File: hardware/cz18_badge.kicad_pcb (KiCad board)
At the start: 2 copper layers, 100 x 100 mm, 16 parts, among them U1 NRF24L01_Breakout

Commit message: Added 433MHz modules
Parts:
- added RF1: RF_Receiver_433_MHz, Sensors:RF_Receiver_433_MHz, F.Cu at (143.5, 44.5)
- added RF2: RF_Transmitter_433_MHz, Sensors:RF_Transmitter_433_MHz, F.Cu at (53.3, 38.1)
- moved U1 54.5 mm to (67.3, 96.5)
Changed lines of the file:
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@@
     (tracks 0)
     (zones 0)
-    (modules 16)
-    (nets 43)
+    (modules 18)
+    (nets 50)
   )
   (page A4)
@@
   (net 41 "Net-(U1-Pad3)")
   (net 42 "Net-(U1-Pad4)")
+  (net 43 "Net-(RF1-Pad1)")
+  (net 44 "Net-(RF1-Pad2)")
+  (net 45 "Net-(RF1-Pad3)")
+  (net 46 "Net-(RF1-Pad4)")
+  (net 47 "Net-(RF2-Pad1)")
+  (net 48 "Net-(RF2-Pad2)")
+  (net 49 "Net-(RF2-Pad3)")
   (net_class Default "This is the default net class."
     (clearance 0.2)
@@
     (add_net "Net-(D3-Pad4)")
     (add_net "Net-(D4-Pad4)")
+    (add_net "Net-(RF1-Pad1)")
+    (add_net "Net-(RF1-Pad2)")
+    (add_net "Net-(RF1-Pad3)")
+    (add_net "Net-(RF1-Pad4)")
+    (add_net "Net-(RF2-Pad1)")
+    (add_net "Net-(RF2-Pad2)")
+    (add_net "Net-(RF2-Pad3)")
     (add_net "Net-(U1-Pad3)")
     (add_net "Net-(U1-Pad4)")
@@
   )
   (module mysensors_radios:NRF24L01 (layer F.Cu)
-    (at 100 140.075001)
+    (at 67.31 96.52)
     (descr NRF24L01)
     (tags "nRF 24 NRF24L01 NRF24L01+")
@@
     )
   )
+  (module Sensors:RF_Receiver_433_MHz (layer F.Cu)
+    (at 143.51 44.45 270)
+    (descr "433 MHz RF Receiver")
+    (tags "rf receiver 433 mhz")
+    (fp_text reference RF1 (at 0 -3 270) (layer F.SilkS)
+      (effects (font (size 1 1) (thickness 0.15)))
+    )
+    (fp_text value RF_Receiver_433_MHz (at 0 3 270) (layer F.Fab)
+      (effects (font (size 1 1) (thickness 0.15)))
+    )
+    (fp_line (start -4.7 -1.1) (end -4.7 -4.6) (layer F.CrtYd) (width 0.15))
+    (fp_line (start -7.4 -1.1) (end -4.7 -1.1) (layer F.CrtYd) (width 0.15))
+    (fp_line (start -7.4 -4.6) (end -7.4 -1.1) (layer F.CrtYd) (width 0.15))
+    (fp_circle (center -20.8 -3) (end -19.6 -2) (layer F.CrtYd) (width 0.15))
+    (fp_line (start 7.58 -4.55) (end 7.58 -5.55) (layer F.CrtYd) (width 0.15))
+    (fp_line (start -22.82 -4.55) (end 7.58 -4.55) (layer F.CrtYd) (width 0.15))
+    (fp_line (start -22.82 -5.54) (end -22.82 -4.55) (layer F.CrtYd) (width 0.15))
+    (fp_line (start 7.58 -5.54) (end -22.82 -5.54) (layer F.CrtYd) (width 0.15))
+    (fp_line (start -3.790707 1.294229) (end 3.829293 1.294229) (layer F.SilkS) (width 0.15))
+    (fp_line (start -3.790707 -1.245771) (end 3.829293 -1.245771) (layer F.SilkS) (width 0.15))
+    (fp_line (start -6.610707 -1.525771) (end -5.060707 -1.525771) (layer F.SilkS) (width 0.15))
+    (fp_line (start 3.829293 1.294229) (end 3.829293 -1.245771) (layer F.SilkS) (width 0.15))
+    (fp_line (start -3.790707 -1.245771) (end -3.790707 1.294229) (layer F.SilkS) (width 0.15))
+    (fp_line (start -5.060707 1.574229) (end -6.610707 1.574229) (layer F.SilkS) (width 0.15))
+    (fp_line (start -6.610707 1.574229) (end -6.610707 -1.525771) (layer F.SilkS) (width 0.15))
+    (pad 1 thru_hole rect (at -5.060707 0.024229) (size 2.032 1.7272) (drill 1.016) (layers *.Cu *.Mask F.SilkS)
+      (net 43 "Net-(RF1-Pad1)"))
+    (pad 2 thru_hole oval (at -2.520707 0.024229) (size 2.032 1.7272) (drill 1.016) (layers *.Cu *.Mask F.SilkS)
+      (net 44 "Net-(RF1-Pad2)"))
+    (pad 3 thru_hole oval (at 0.019293 0.024229) (size 2.032 1.7272) (drill 1.016) (layers *.Cu *.Mask F.SilkS)
+      (net 45 "Net-(RF1-Pad3)"))
+    (pad 4 thru_hole oval (at 2.559293 0.024229) (size 2.032 1.7272) (drill 1.016) (layers *.Cu *.Mask F.SilkS)
+      (net 46 "Net-(RF1-Pad4)"))
+    (model Pin_Headers.3dshapes/Pin_Header_Straight_1x04.wrl
+      (at (xyz 0 -0.15 0))
+      (scale (xyz 1 1 1))
+      (rotate (xyz 0 0 90))
+    )
+  )
+  (module Sensors:RF_Transmitter_433_MHz (layer F.Cu)
+    (at 53.34 38.1 90)
+    (fp_text reference RF2 (at 0 4.445 90) (layer F.SilkS)
+      (effects (font (size 1 1) (thickness 0.15)))
+    )
+    (fp_text value RF_Transmitter_433_MHz (at 0 2.54 90) (layer F.Fab)
+      (effects (font (size 1 1) (thickness 0.15)))
+    )
+    (fp_line (start 3.81 1.27) (end -1.27 1.27) (layer F.SilkS) (width 0.15))
+    (fp_line (start 3.81 -1.27) (end 3.81 1.27) (layer F.SilkS) (width 0.15))
+    (fp_line (start -1.27 -1.27) (end 3.81 -1.27) (layer F.SilkS) (width 0.15))
+    (fp_line (start -1.27 1.27) (end -1.27 -1.27) (layer F.SilkS) (width 0.15))
+    (fp_line (start -4.064 1.524) (end -2.54 1.524) (layer F.SilkS) (width 0.15))
+    (fp_line (start -4.064 -1.524) (end -4.064 1.524) (layer F.SilkS) (width 0.15))
+    (fp_line (start -2.54 -1.524) (end -4.064 -1.524) (layer F.SilkS) (width 0.15))
+    (fp_line (start -4.445 0.635) (end -4.445 -0.635) (layer F.CrtYd) (width 0.15))
+    (fp_line (start -6.985 0.635) (end -4.445 0.635) (layer F.CrtYd) (width 0.15))
+    (fp_line (start -6.985 -0.635) (end -6.985 0.635) (layer F.CrtYd) (width 0.15))
+    (fp_line (start 9.525 -0.635) (end -9.525 -0.635) (layer F.CrtYd) (width 0.15))
+    (fp_line (start 9.525 -1.905) (end 9.525 -0.635) (layer F.CrtYd) (width 0.15))
+    (fp_line (start -9.525 -1.905) (end 9.525 -1.905) (layer F.CrtYd) (width 0.15))
+    (fp_line (start -9.525 -0.635) (end -9.525 -1.905) (layer F.CrtYd) (width 0.15))
+    (pad 1 thru_hole rect (at -2.54 0 180) (size 2.032 1.7272) (drill 1.016) (layers *.Cu *.Mask F.SilkS)
+      (net 47 "Net-(RF2-Pad1)"))
+    (pad 2 thru_hole oval (at 0 0 180) (size 2.032 1.7272) (drill 1.016) (layers *.Cu *.Mask F.SilkS)
+      (net 48 "Net-(RF2-Pad2)"))
+    (pad 3 thru_hole oval (at 2.54 0 180) (size 2.032 1.7272) (drill 1.016) (layers *.Cu *.Mask F.SilkS)
+      (net 49 "Net-(RF2-Pad3)"))
+  )
   (gr_text "TODO:\n\n- Finalise PCB design concept\n- Layout components\n- Create VCC and GND planes on front and back of the badge\n- Route traces" (at 186 53) (layer F.Cu)

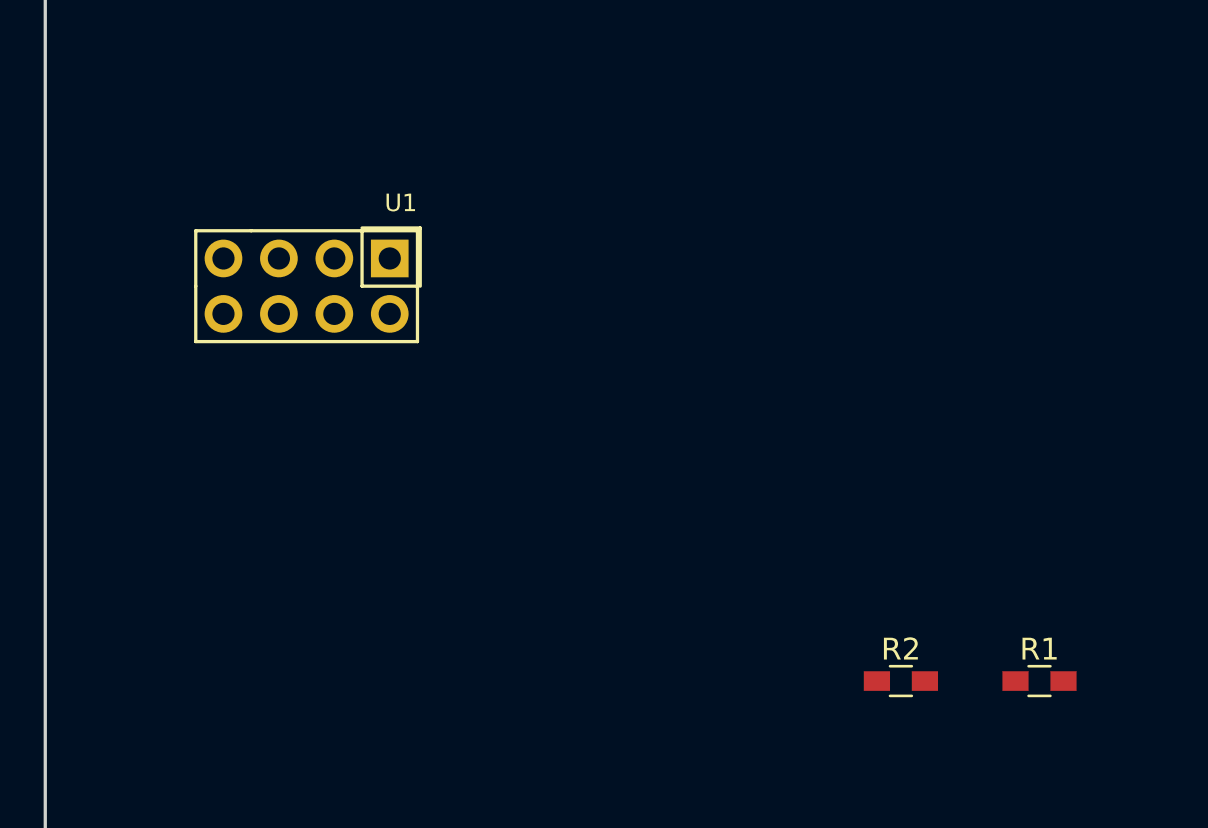
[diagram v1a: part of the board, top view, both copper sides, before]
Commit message: Connected component labels
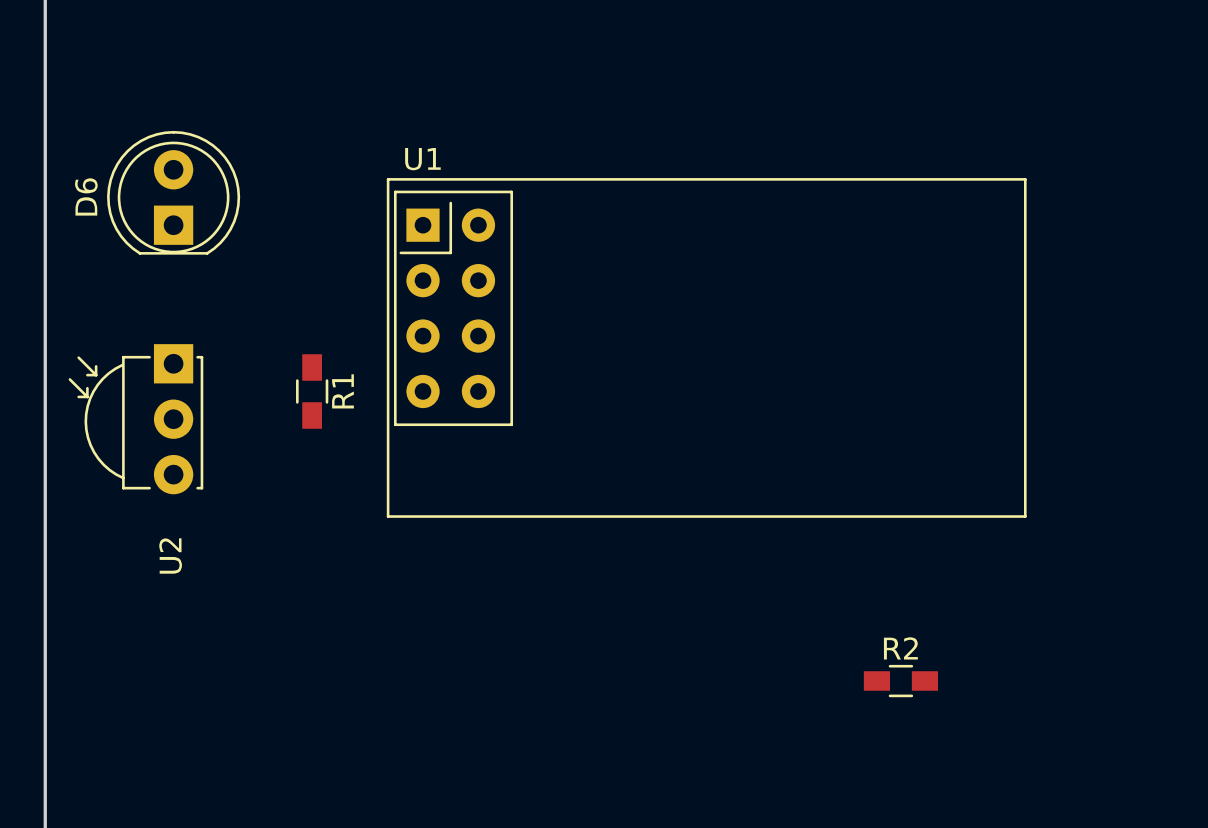
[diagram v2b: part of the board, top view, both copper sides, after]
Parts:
- added D6: LD271, LEDs:LED_D5.0mm, F.Cu at (55.9, 96.5)
- added U2: TSOP323xx, Opto-Devices:IRReceiver_Vishay_MOLD-3pin, F.Cu at (55.9, 102.9)
- R1: value 0k -> 10k
- U1: footprint mysensors_radios:NRF24L01 -> RF_Modules:nRF24L01_Breakout
- moved R1 35.9 mm to (62.2, 104.1), turned to 270 degrees
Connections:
- A1 pad 10: Net-(A1-Pad10) -> IR_RECV
- A1 pad 11: Net-(A1-Pad11) -> RF_SEND
- A1 pad 12: BUZZ1 -> SPI_CE
- A1 pad 13: BUZZ2 -> SPI_CS
- A1 pad 14: Net-(A1-Pad14) -> SPI_MOSI
- A1 pad 15: Net-(A1-Pad15) -> SPI_MISO
- A1 pad 16: Net-(A1-Pad16) -> SPI_SCK
- A1 pad 5: Net-(A1-Pad5) -> RF_RECV
- A1 pad 6: Net-(A1-Pad6) -> IR_SEND
- A1 pad 7: Net-(A1-Pad7) -> LEDS_IN
- A1 pad 8: Net-(A1-Pad8) -> BUZZ1
- A1 pad 9: Net-(A1-Pad9) -> BUZZ2
- R1 pad 1: VCC -> IR_RECV
- R1 pad 2: Net-(A1-Pad30) -> VCC
- RF1 pad 1: Net-(RF1-Pad1) -> VCC
- RF1 pad 2: Net-(RF1-Pad2) -> RF_RECV
- RF1 pad 3: Net-(RF1-Pad3) -> RF_RECV
- RF1 pad 4: Net-(RF1-Pad4) -> GNDREF
- RF2 pad 1: Net-(RF2-Pad1) -> RF_SEND
- RF2 pad 2: Net-(RF2-Pad2) -> VCC
- RF2 pad 3: Net-(RF2-Pad3) -> GNDREF
- U1 pad 3: Net-(U1-Pad3) -> SPI_CE
- U1 pad 4: Net-(U1-Pad4) -> SPI_CS
- U1 pad 5: Net-(U1-Pad5) -> SPI_SCK
- U1 pad 6: Net-(U1-Pad6) -> SPI_MOSI
- U1 pad 7: Net-(U1-Pad7) -> SPI_MISO

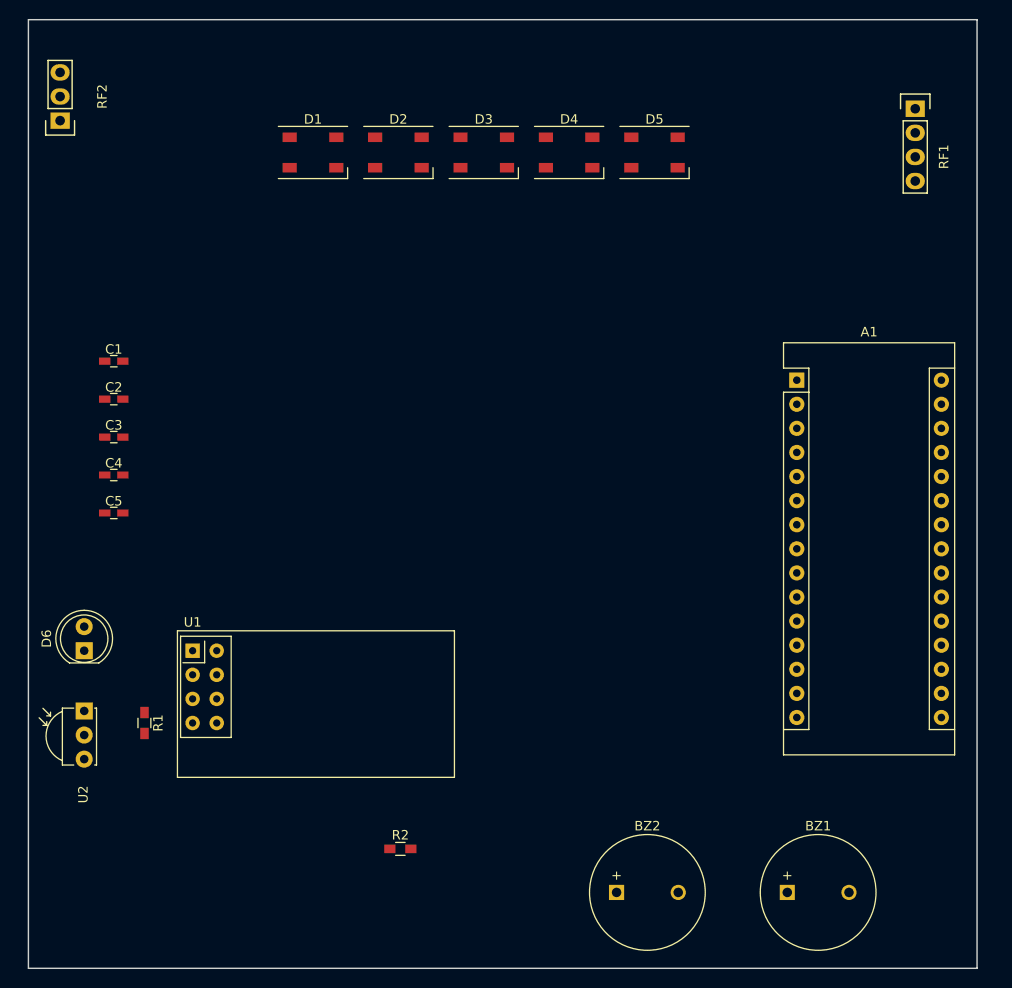
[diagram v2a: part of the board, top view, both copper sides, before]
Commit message: Added battery and dev breakout, routed dev traces on test PCB
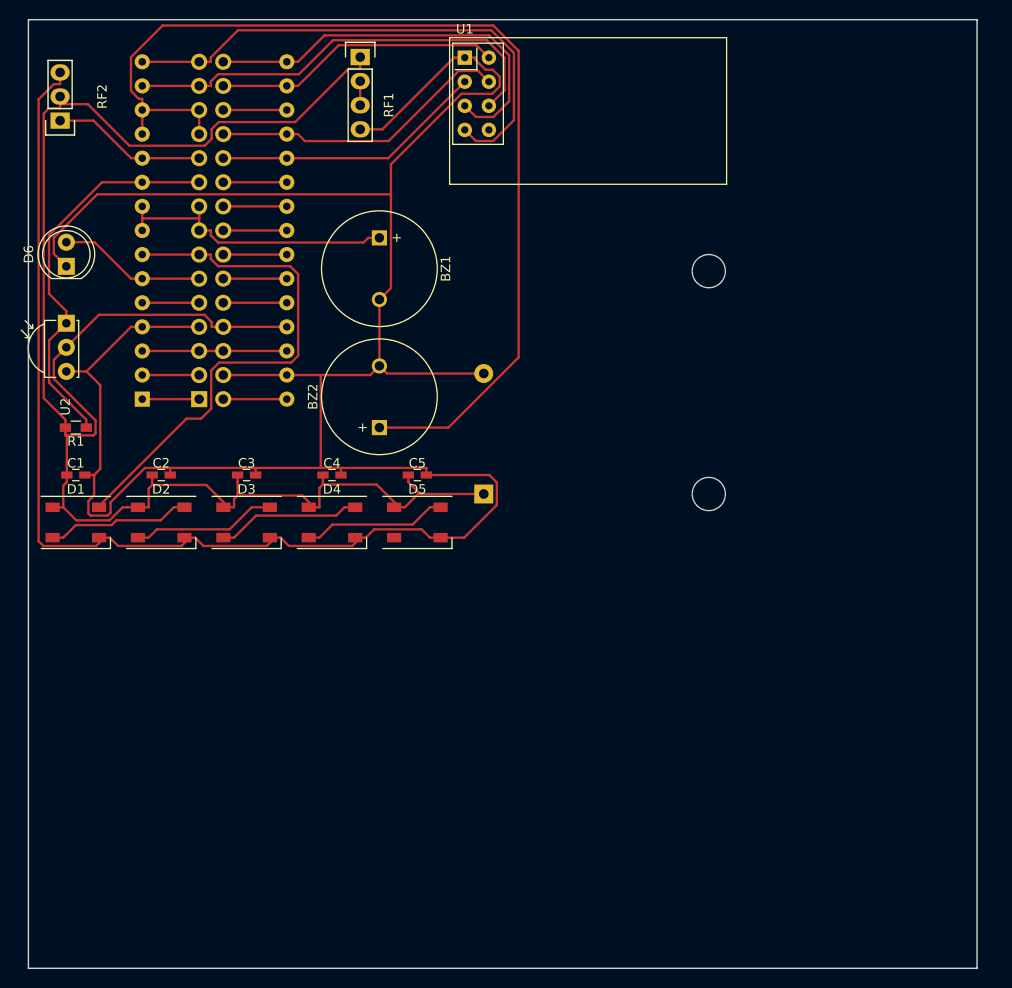
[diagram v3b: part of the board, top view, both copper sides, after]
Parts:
- removed R2: 0k, Resistors_SMD:R_0603_HandSoldering
- added BT1: Battery, Battery_Holders:Keystone_2479_3xAAA, B.Cu at (98.0, 80.0)
- added J1: Dev breakout, Pin_Headers:Pin_Header_Straight_2x15_Pitch2.54mm, B.Cu at (68.0, 70.0)
- A1: moved to B.Cu
- D6: value LD271 -> 940nm
- RF1: value RF_Receiver_433_MHz -> 433MHz Receiver
- RF2: value RF_Transmitter_433_MHz -> 433MHz Transmitter
- U1: value NRF24L01_Breakout -> NRF24L01
- U2: value TSOP323xx -> CHQ1838
- moved BZ1 81.3 mm to (87.0, 53.0), turned to 270 degrees
- moved A1 69.0 mm to (62.0, 70.0)
- moved U1 68.8 mm to (96.0, 34.0)
- moved RF1 58.8 mm to (85.0, 39.0)
- moved BZ2 55.0 mm to (87.0, 73.0), turned to 90 degrees
- moved D1 46.3 mm to (55.0, 83.0)
- moved D2 46.3 mm to (64.0, 83.0)
- moved D3 46.3 mm to (73.0, 83.0)
- moved D4 46.3 mm to (82.0, 83.0)
- moved D5 46.3 mm to (91.0, 83.0)
- moved U2 40.9 mm to (54.0, 62.0)
- moved D6 40.6 mm to (54.0, 56.0)
- moved C5 32.2 mm to (91.0, 78.0)
- moved R1 32.0 mm to (55.0, 73.0), turned to 180 degrees
- moved C4 23.0 mm to (82.0, 78.0)
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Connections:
- net GNDREF renamed GND
- net IR_RECV renamed D7
- net IR_SEND renamed D3
- net LEDS_IN renamed D4
- net RF_RECV renamed D2
- net RF_SEND renamed D8
- net SPI_MISO renamed D12
- net SPI_MOSI renamed D11
- net SPI_SCK renamed D13
- A1 pad 1: Net-(A1-Pad1) -> TX
- A1 pad 12: SPI_CE -> BUZZ2
- A1 pad 13: SPI_CS -> BUZZ2
- A1 pad 17: Net-(A1-Pad17) -> 3V3
- A1 pad 18: Net-(A1-Pad18) -> AREF
- A1 pad 19: Net-(A1-Pad19) -> A0
- A1 pad 2: Net-(A1-Pad2) -> RX
- A1 pad 20: Net-(A1-Pad20) -> A1
- A1 pad 21: Net-(A1-Pad21) -> A2
- A1 pad 22: Net-(A1-Pad22) -> A3
- A1 pad 23: Net-(A1-Pad23) -> A4
- A1 pad 24: Net-(A1-Pad24) -> A5
- A1 pad 25: Net-(A1-Pad25) -> A6
- A1 pad 26: Net-(A1-Pad26) -> A7
- A1 pad 27: Net-(A1-Pad27) -> VCC
- A1 pad 28: Net-(A1-Pad28) -> RESET
- A1 pad 3: Net-(A1-Pad3) -> RESET
- A1 pad 30: Net-(A1-Pad30) -> VIN
- A1 pad 9: BUZZ2 -> BUZZ1
- D5 pad 4: LEDS_OUT -> (no net)
- U1 pad 2: VCC -> 3V3
- U1 pad 3: SPI_CE -> A1
- U1 pad 4: SPI_CS -> A0
- U1 pad 8: Net-(U1-Pad8) -> (no net)
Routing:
- net GND: track 0.00 -> 326.2 mm
- net VCC: track 0.00 -> 188.0 mm
- net BUZZ2: track 0.00 -> 111.0 mm
- net D4: track 0.00 -> 56.2 mm
- net D12: track 0.00 -> 55.5 mm
- net D11: track 0.00 -> 46.9 mm
- net D13: track 0.00 -> 42.8 mm
- net D7: track 0.00 -> 41.5 mm
- net A0: track 0.00 -> 31.8 mm
- net BUZZ1: track 0.00 -> 31.1 mm
- net 3V3: track 0.00 -> 30.3 mm
- net A1: track 0.00 -> 28.8 mm
- net D8: track 0.00 -> 16.3 mm
- net D3: track 0.00 -> 15.6 mm
- net RESET: track 0.00 -> 15.2 mm
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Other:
- net class Default: clearance 0.2 -> 0.25
- rule trace_clearance: 0.2 -> 0.25
